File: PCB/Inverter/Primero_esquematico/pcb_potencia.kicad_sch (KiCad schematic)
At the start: 0 parts

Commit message: correcciones de apps
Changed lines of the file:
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@@
-	(wire
-		(pts
-			(xy 119.38 82.55) (xy 120.65 82.55)
-		)
-		(stroke
-			(width 0)
-			(type default)
-		)
-	)
 	(wire
 		(pts

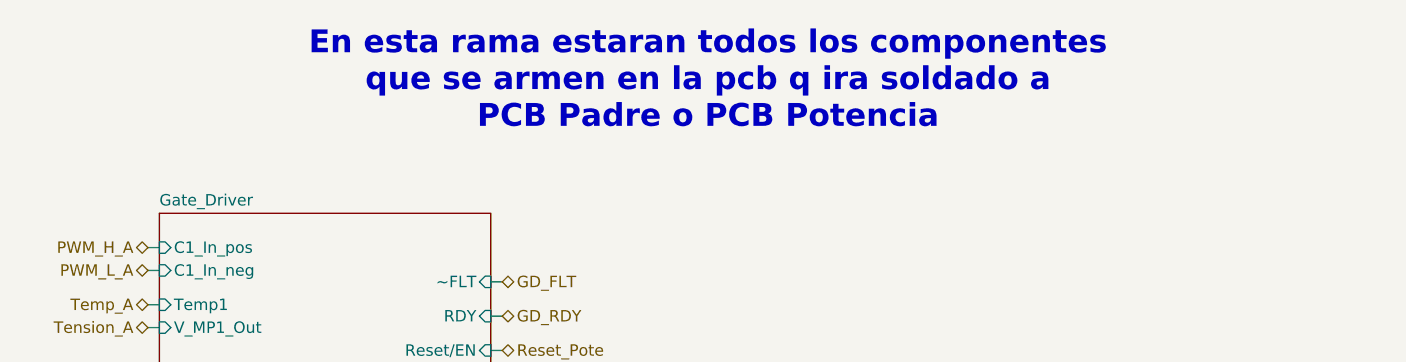
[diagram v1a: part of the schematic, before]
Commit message: EsqumaticoCuasifinalizado
Ya hice varias correcciones creo q solo falta cambiar algunas resistencias en los limites q tendrian que estar en el notion
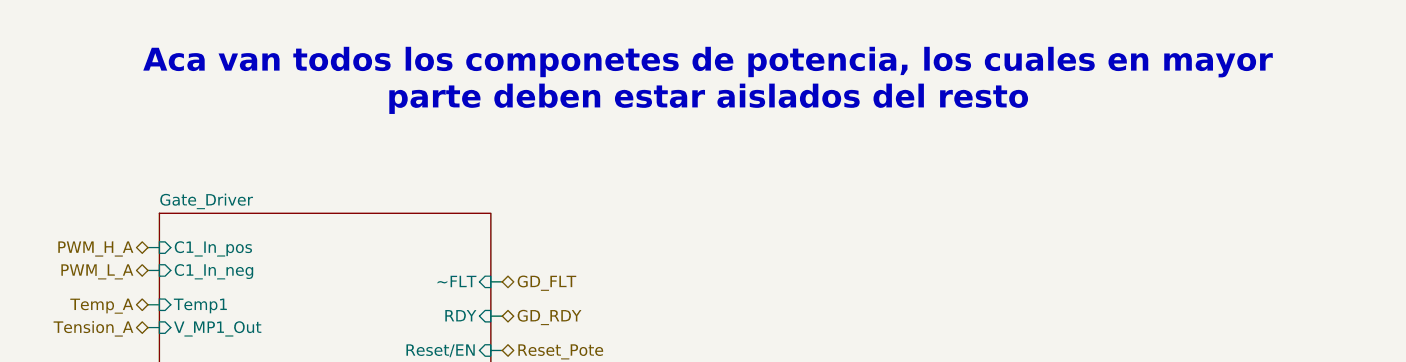
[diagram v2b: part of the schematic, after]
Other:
- note added: "Aca van todos los componetes de potencia, los cuales en mayor parte deben estar aislados del resto"
- note removed: "En esta rama estaran todos los componentes que se armen en la pcb q ira soldado a PCB Padre o PCB Potencia"
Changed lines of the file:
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@@
 	(generator_version "10.0")
 	(paper "A4")
-	(text "En esta rama estaran todos los componentes\nque se armen en la pcb q ira soldado a\nPCB Padre o PCB Potencia"
+	(text "Aca van todos los componetes de potencia, los cuales en mayor\nparte deben estar aislados del resto"
 		(exclude_from_sim no)
 		(at 143.51 48.768 0)

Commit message: Modificaciones por falta de stock
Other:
- sheet currentS ports: added I_MCU_1, I_MCU_2, I_MCU_3, OCD; removed Uot1, Uot2, Uot3
